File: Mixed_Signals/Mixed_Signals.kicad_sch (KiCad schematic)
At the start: 0 parts

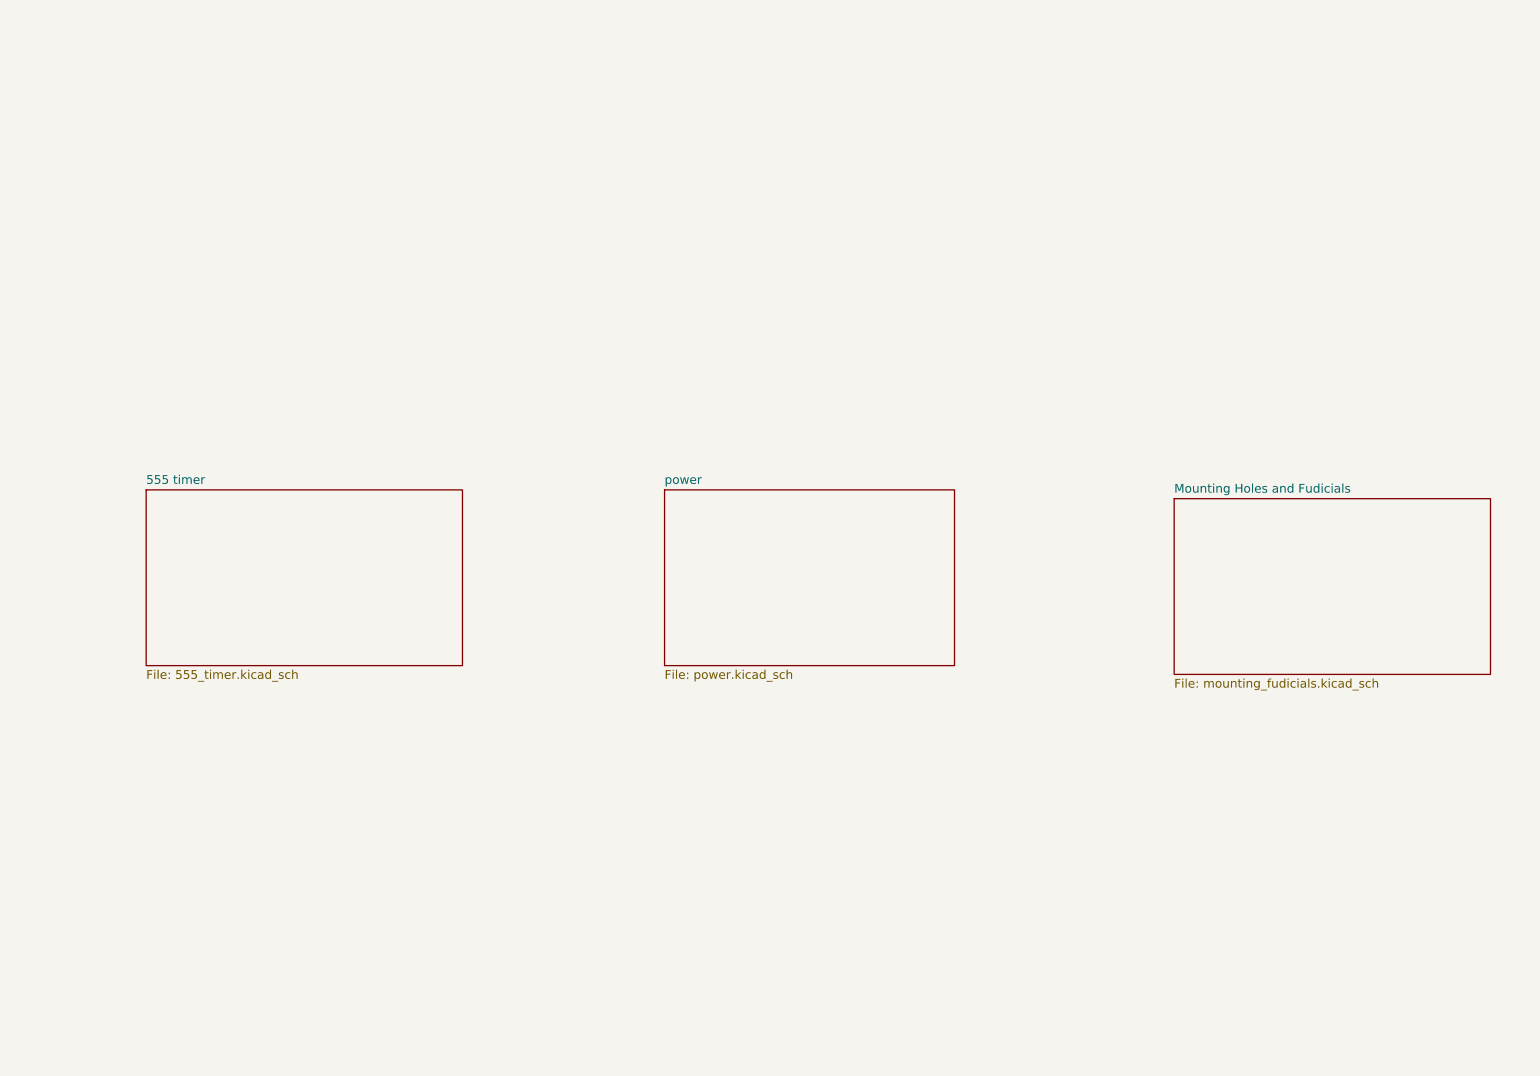
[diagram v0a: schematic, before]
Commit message: added logo library
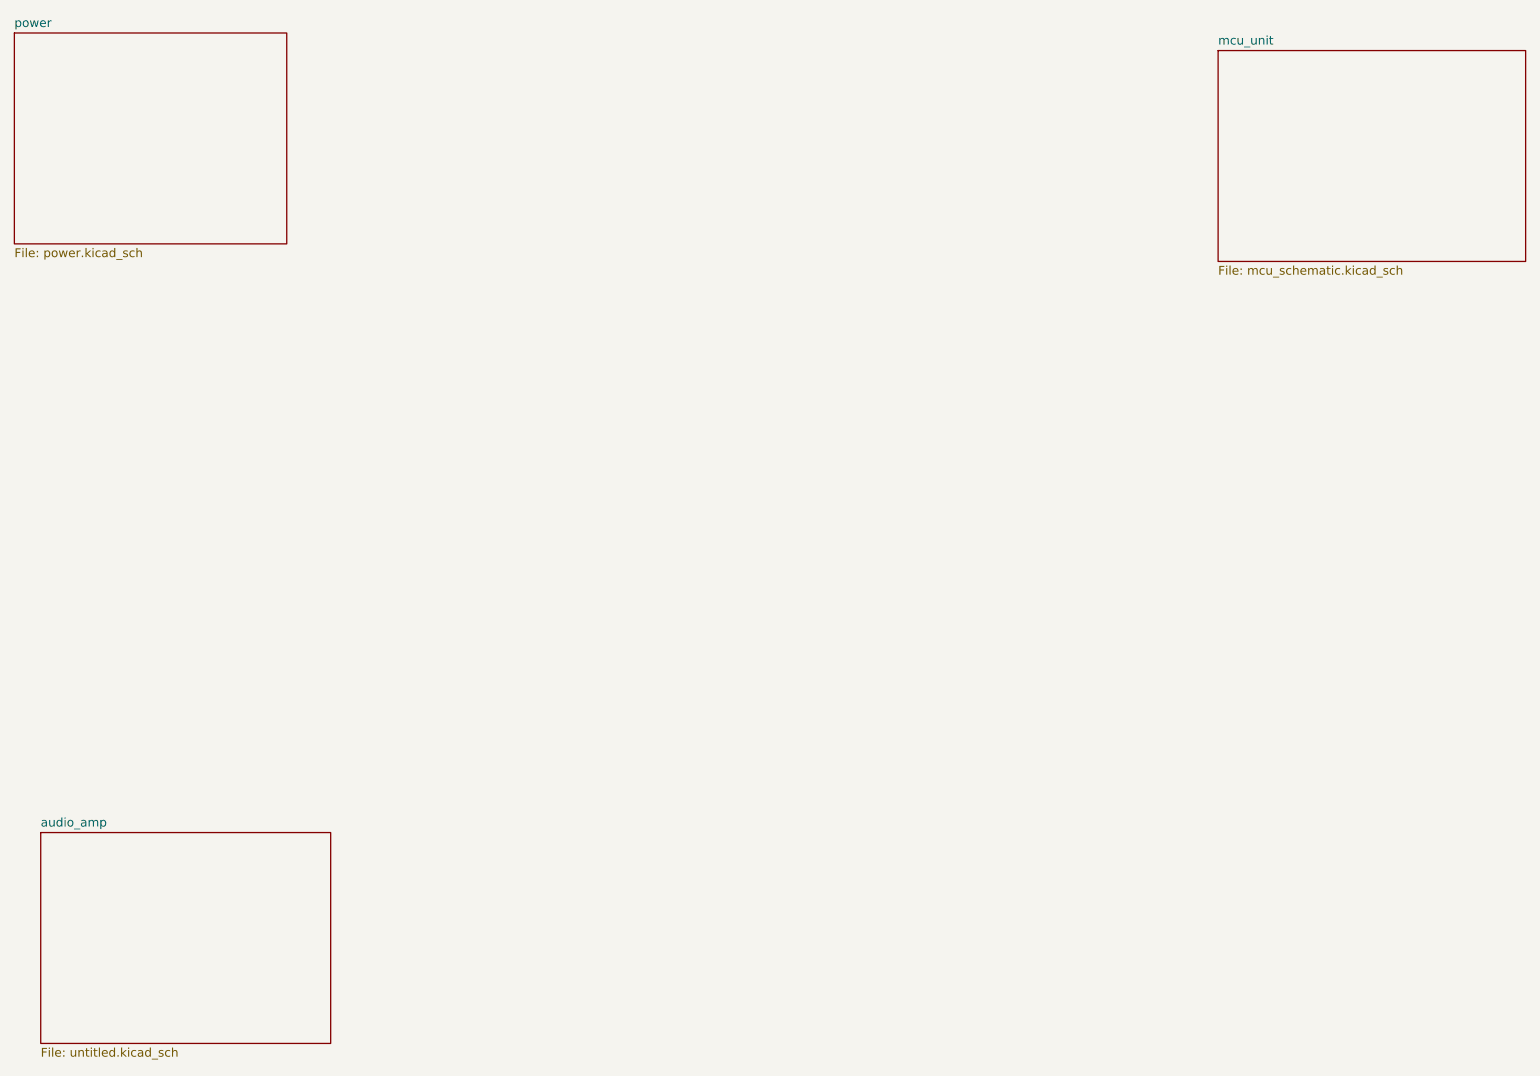
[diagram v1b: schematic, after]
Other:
- removed sheet 555 timer
- removed sheet Mounting Holes and Fudicials
- added sheet audio_amp (untitled.kicad_sch)
- added sheet mcu_unit (mcu_schematic.kicad_sch)
- company: Pilolo -> (none)
- title: 555 Astable Multivibrator -> (none)
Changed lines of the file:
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@@
 	(generator_version "9.0")
 	(paper "A4")
-	(title_block
-		(title "555 Astable Multivibrator")
-		(date "2025-10-30")
-		(rev "V1.0")
-		(company "Pilolo")
-		(comment 1 "Test Project")
-	)
 	(sheet
-		(at 48.26 95.25)
-		(size 45.72 25.4)
+		(at 33.02 144.78)
+		(size 41.91 30.48)
 		(exclude_from_sim no)
 		(in_bom yes)
@@
 			(color 0 0 0 0.0000)
 		)
-		(property "Sheetname" "555 timer"
-			(at 48.26 94.5384 0)
+		(property "Sheetname" "audio_amp"
+			(at 33.02 144.0684 0)
 			(effects
 				(font
@@
 			)
 		)
-		(property "Sheetfile" "555_timer.kicad_sch"
-			(at 48.26 121.2346 0)
+		(property "Sheetfile" "untitled.kicad_sch"
+			(at 33.02 175.8446 0)
 			(effects
 				(font
@@
 		)
 		(instances
-			(project "DrawSchematic"
-				(path "/65fc31cb-d80e-4d8e-8c07-0f1fb5255ca3"
-					(page "2")
+			(project "Mixed_Signals"
+				(path "/2e22a617-e9e9-4deb-b0d2-03da1faa5147"
+					(page "3")
 				)
 			)
@@
 	)
 	(sheet
-		(at 196.85 96.52)
-		(size 45.72 25.4)
+		(at 203.2 31.75)
+		(size 44.45 30.48)
 		(exclude_from_sim no)
 		(in_bom yes)
@@
 			(color 0 0 0 0.0000)
 		)
-		(property "Sheetname" "Mounting Holes and Fudicials"
-			(at 196.85 95.8084 0)
+		(property "Sheetname" "mcu_unit"
+			(at 203.2 31.0384 0)
 			(effects
 				(font
@@
 			)
 		)
-		(property "Sheetfile" "mounting_fudicials.kicad_sch"
-			(at 196.85 122.5046 0)
+		(property "Sheetfile" "mcu_schematic.kicad_sch"
+			(at 203.2 62.8146 0)
 			(effects
 				(font
@@
 		)
 		(instances
-			(project "DrawSchematic"
-				(path "/65fc31cb-d80e-4d8e-8c07-0f1fb5255ca3"
+			(project "Mixed_Signals"
+				(path "/2e22a617-e9e9-4deb-b0d2-03da1faa5147"
 					(page "4")
 				)
@@
 	)
 	(sheet
-		(at 123.19 95.25)
-		(size 41.91 25.4)
+		(at 29.21 29.21)
+		(size 39.37 30.48)
 		(exclude_from_sim no)
 		(in_bom yes)
@@
 		)
 		(property "Sheetname" "power"
-			(at 123.19 94.5384 0)
+			(at 29.21 28.4984 0)
 			(effects
 				(font
@@
 		)
 		(property "Sheetfile" "power.kicad_sch"
-			(at 123.19 121.2346 0)
+			(at 29.21 60.2746 0)
 			(effects
 				(font
@@
 		)
 		(instances
-			(project "DrawSchematic"
-				(path "/65fc31cb-d80e-4d8e-8c07-0f1fb5255ca3"
-					(page "3")
+			(project "Mixed_Signals"
+				(path "/2e22a617-e9e9-4deb-b0d2-03da1faa5147"
+					(page "2")
 				)
 			)

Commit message: cleaned up
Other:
- removed sheet audio_amp
- added sheet amplifier_sch (amplifier_sch.kicad_sch)
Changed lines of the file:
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@@
 	(paper "A4")
-	(sheet
-		(at 33.02 144.78)
-		(size 41.91 30.48)
-		(exclude_from_sim no)
-		(in_bom yes)
-		(on_board yes)
-		(dnp no)
-		(fields_autoplaced yes)
-		(stroke
-			(width 0.1524)
-			(type solid)
-		)
-		(fill
-			(color 0 0 0 0.0000)
-		)
-		(property "Sheetname" "audio_amp"
-			(at 33.02 144.0684 0)
-			(effects
-				(font
-					(size 1.27 1.27)
-				)
-				(justify left bottom)
-			)
-		)
-		(property "Sheetfile" "untitled.kicad_sch"
-			(at 33.02 175.8446 0)
-			(effects
-				(font
-					(size 1.27 1.27)
-				)
-				(justify left top)
-			)
-		)
-		(instances
-			(project "Mixed_Signals"
-				(path "/2e22a617-e9e9-4deb-b0d2-03da1faa5147"
-					(page "3")
-				)
-			)
-		)
-	)
 	(sheet
 		(at 203.2 31.75)
@@
 			(effects
 				(font
+					(size 1.27 1.27)
+				)
+				(justify left top)
+			)
+		)
+		(instances
+			(project "Mixed_Signals"
+				(path "/2e22a617-e9e9-4deb-b0d2-03da1faa5147"
+					(page "4")
+				)
+			)
+		)
+	)
+	(sheet
+		(at 35.56 124.46)
+		(size 46.99 33.02)
+		(exclude_from_sim no)
+		(in_bom yes)
+		(on_board yes)
+		(dnp no)
+		(fields_autoplaced yes)
+		(stroke
+			(width 0.1524)
+			(type solid)
+		)
+		(fill
+			(color 0 0 0 0.0000)
+		)
+		(property "Sheetname" "amplifier_sch"
+			(at 35.56 123.7484 0)
+			(effects
+				(font
+					(size 1.27 1.27)
+				)
+				(justify left bottom)
+			)
+		)
+		(property "Sheetfile" "amplifier_sch.kicad_sch"
+			(at 35.56 158.0646 0)
+			(effects
+				(font
